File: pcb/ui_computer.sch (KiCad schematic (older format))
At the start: 9 parts

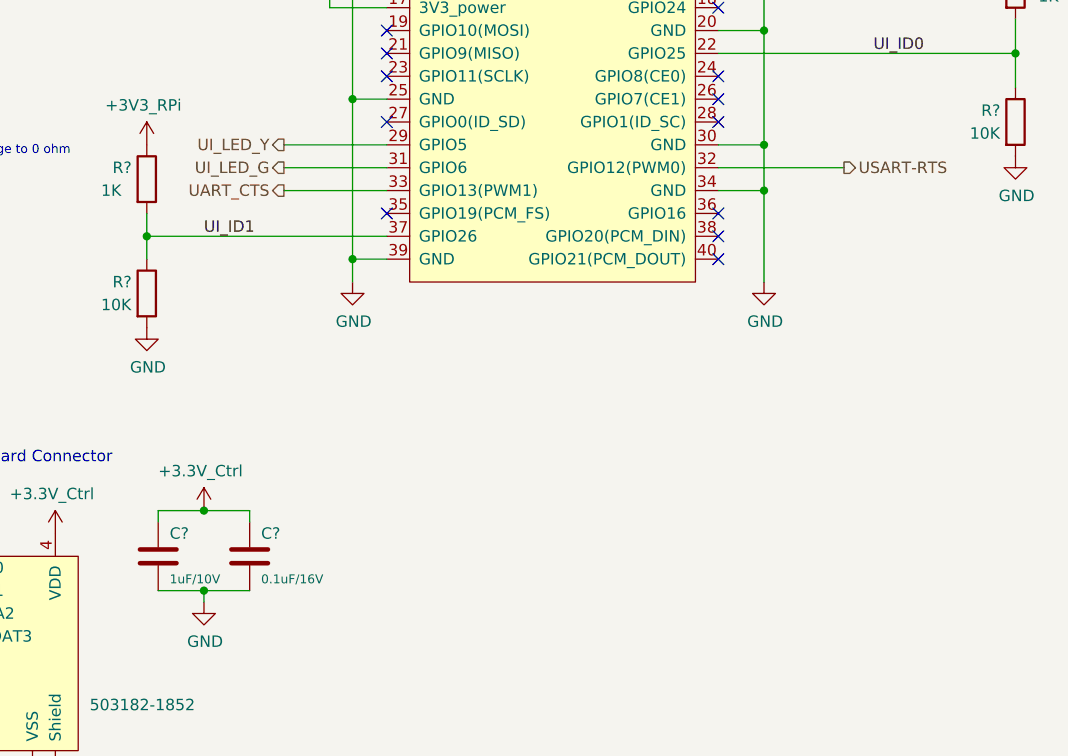
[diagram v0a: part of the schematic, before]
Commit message: change some I/Os
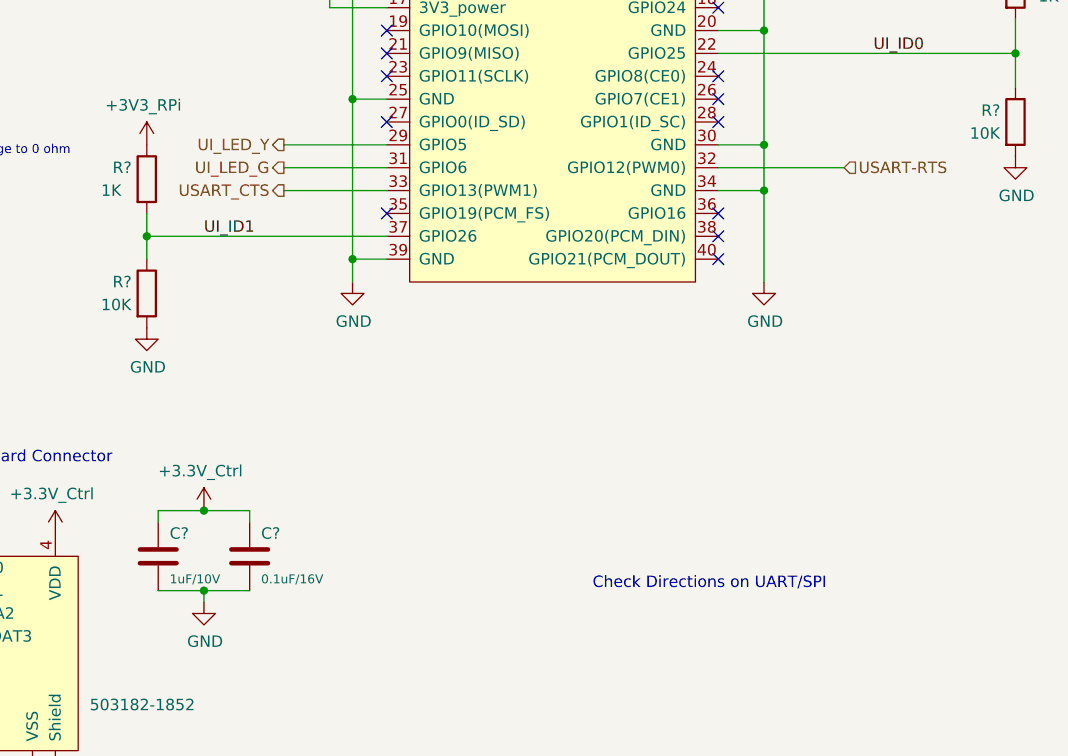
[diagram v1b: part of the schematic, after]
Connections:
- net labels added: USART_CTS
- net labels removed: UART_CTS
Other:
- note added: "Check Directions on UART/SPI"
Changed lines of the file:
@@
 RPI powered by 5V\n
 Text HLabel 4550 3900 0    50   Output ~ 0
-UART_CTS
+USART_CTS
 Wire Wire Line
 	5000 3900 4550 3900
@@
 Wire Wire Line
 	6450 3800 7000 3800
-Text HLabel 7000 3800 2    50   Output ~ 0
+Text HLabel 7000 3800 2    50   Input ~ 0
 USART-RTS
 $Comp
@@
 Text HLabel 2700 6050 0    50   Input ~ 0
 USD-SCLK
+Text Notes 5900 5650 0    50   ~ 0
+Check Directions on UART/SPI
 $EndSCHEMATC

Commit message: started stm
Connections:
- net labels added: +5V_GUI
- net labels removed: +5V_RPi
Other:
- note removed: "RPI has internal I2C pull-ups\n"
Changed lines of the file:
@@
 	1    0    0    -1
 $EndComp
-Text Notes 5200 1950 0    50   ~ 0
-RPI has internal I2C pull-ups\n
 NoConn ~ 5000 2400
 NoConn ~ 5000 2500
@@
 NoConn ~ 5000 3600
 NoConn ~ 5000 4000
-$Comp
-L RespiraWorks:+5V_RPi #PWR?
-U 1 1 5FE675EB
-P 6750 2300
-F 0 "#PWR?" H 6750 2300 50  0001 C CNN
-F 1 "+5V_RPi" H 6735 2473 50  0000 C CNN
-F 2 "" H 6750 2300 50  0001 C CNN
-F 3 "" H 6750 2300 50  0001 C CNN
-	1    6750 2300
-	1    0    0    -1
-$EndComp
 Wire Wire Line
 	6450 2300 6750 2300
@@
 Wire Wire Line
 	6750 2400 6750 2300
-Connection ~ 6750 2300
 Wire Wire Line
 	6650 4300 6650 3900
@@
 Text Notes 5900 5650 0    50   ~ 0
 Check Directions on UART/SPI
+$Comp
+L RespiraWorks:+5V_GUI #PWR?
+U 1 1 5FEBC42B
+P 6750 2300
+F 0 "#PWR?" H 6750 2300 50  0001 C CNN
+F 1 "+5V_GUI" H 6735 2473 50  0000 C CNN
+F 2 "" H 6750 2300 50  0001 C CNN
+F 3 "" H 6750 2300 50  0001 C CNN
+	1    6750 2300
+	1    0    0    -1
+$EndComp
+Connection ~ 6750 2300
 $EndSCHEMATC

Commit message: most up to date
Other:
- note added: "Place USB to UART for FPGA comms"
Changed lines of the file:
@@
 $EndComp
 Connection ~ 6750 2300
+Text Notes 2450 1850 0    50   ~ 0
+Place USB to UART for FPGA comms
 $EndSCHEMATC

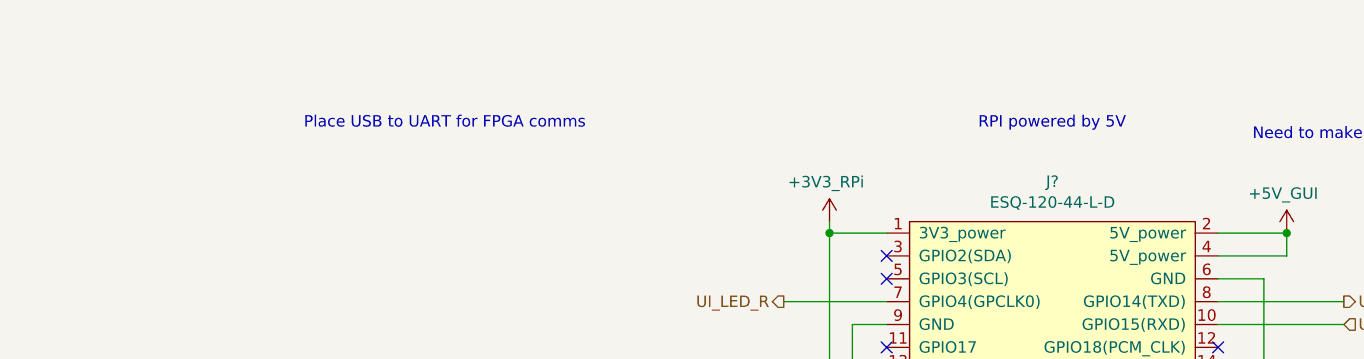
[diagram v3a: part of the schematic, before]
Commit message: updated cycle controller
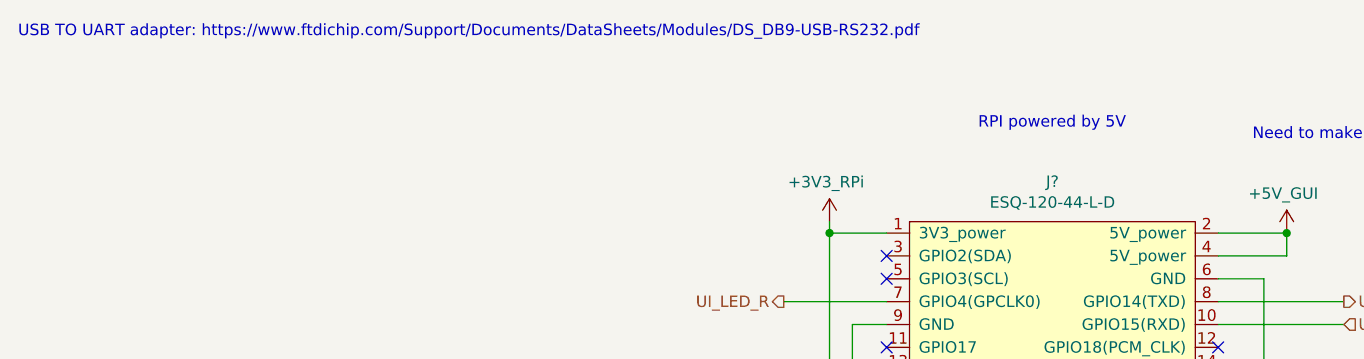
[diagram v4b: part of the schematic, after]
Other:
- note added: "USB TO UART adapter: https://www.ftdichip.com/Support/Documents/DataSheets/Modules/DS_DB9-USB-RS232.pdf"
- note removed: "Place USB to UART for FPGA comms"
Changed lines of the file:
@@
 $Descr A4 11693 8268
 encoding utf-8
-Sheet 14 14
+Sheet 6 28
 Title "UI Computer"
 Date ""
@@
 $EndComp
 Connection ~ 6750 2300
-Text Notes 2450 1850 0    50   ~ 0
-Place USB to UART for FPGA comms
+Text Notes 1200 1450 0    50   ~ 0
+USB TO UART adapter: https://www.ftdichip.com/Support/Documents/DataSheets/Modules/DS_DB9-USB-RS232.pdf
 $EndSCHEMATC

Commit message: some cycle controller updates- more to come shortly
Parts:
- removed C?: 1uF/10V, symbol Device:C
- removed C?: 0.1uF/16V, symbol Device:C
- removed J?: 503182-1852, RespiraWorks:5031821852, symbol RespiraWorks:503182-1852
- removed R?: 10K, RespiraWorks_std:R_0603_1608Metric, symbol Device:R
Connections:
- no-connect marks 21 -> 18
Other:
- note removed: "Check Directions on UART/SPI"
- note removed: "Double Check sw/dt footprint"
- note removed: "MicroSD Card Connector"
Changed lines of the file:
@@
 USART-RTS
-$Comp
-L RespiraWorks:503182-1852 J?
-U 1 1 5FE6F067
-P 3350 5800
-F 0 "J?" H 3150 6150 50  0000 L CNN
-F 1 "503182-1852" H 3700 5450 50  0000 L CNN
-F 2 "RespiraWorks:5031821852" H 4150 5400 50  0001 C CNN
-F 3 "https://www.molex.com/pdm_docs/sd/5031821852_sd.pdf" H 4750 5300 50  0001 C CNN
-	1    3350 5800
-	1    0    0    -1
-$EndComp
-Text Notes 3800 5100 2    50   ~ 0
-MicroSD Card Connector
-$Comp
-L RespiraWorks:+3.3V_Ctrl #PWR?
-U 1 1 5FE6F137
-P 3550 5400
-F 0 "#PWR?" H 3550 5400 50  0001 C CNN
-F 1 "+3.3V_Ctrl" H 3535 5573 50  0000 C CNN
-F 2 "" H 3550 5400 50  0001 C CNN
-F 3 "" H 3550 5400 50  0001 C CNN
-	1    3550 5400
-	1    0    0    -1
-$EndComp
-$Comp
-L Device:C C?
-U 1 1 5FE6F180
-P 4000 5500
-F 0 "C?" H 4050 5600 50  0000 L CNN
-F 1 "1uF/10V" H 4050 5400 39  0000 L CNN
-F 2 "" H 4038 5350 50  0001 C CNN
-F 3 "~" H 4000 5500 50  0001 C CNN
-	1    4000 5500
-	1    0    0    -1
-$EndComp
-$Comp
-L Device:C C?
-U 1 1 5FE6F1C6
-P 4400 5500
-F 0 "C?" H 4450 5600 50  0000 L CNN
-F 1 "0.1uF/16V" H 4450 5400 39  0000 L CNN
-F 2 "" H 4438 5350 50  0001 C CNN
-F 3 "~" H 4400 5500 50  0001 C CNN
-	1    4400 5500
-	1    0    0    -1
-$EndComp
-$Comp
-L RespiraWorks:+3.3V_Ctrl #PWR?
-U 1 1 5FE6F2AB
-P 4200 5300
-F 0 "#PWR?" H 4200 5300 50  0001 C CNN
-F 1 "+3.3V_Ctrl" H 4185 5473 50  0000 C CNN
-F 2 "" H 4200 5300 50  0001 C CNN
-F 3 "" H 4200 5300 50  0001 C CNN
-	1    4200 5300
-	1    0    0    -1
-$EndComp
-Wire Wire Line
-	4000 5350 4000 5300
-Wire Wire Line
-	4000 5300 4200 5300
-Wire Wire Line
-	4200 5300 4400 5300
-Wire Wire Line
-	4400 5300 4400 5350
-Connection ~ 4200 5300
-$Comp
-L power:GND #PWR?
-U 1 1 5FE705DA
-P 4200 5700
-F 0 "#PWR?" H 4200 5450 50  0001 C CNN
-F 1 "GND" H 4205 5527 50  0000 C CNN
-F 2 "" H 4200 5700 50  0001 C CNN
-F 3 "" H 4200 5700 50  0001 C CNN
-	1    4200 5700
-	1    0    0    -1
-$EndComp
-Wire Wire Line
-	4000 5650 4200 5650
-Wire Wire Line
-	4200 5650 4200 5700
-Wire Wire Line
-	4400 5650 4200 5650
-Connection ~ 4200 5650
-$Comp
-L power:GND #PWR?
-U 1 1 5FE71557
-P 3500 6500
-F 0 "#PWR?" H 3500 6250 50  0001 C CNN
-F 1 "GND" H 3505 6327 50  0000 C CNN
-F 2 "" H 3500 6500 50  0001 C CNN
-F 3 "" H 3500 6500 50  0001 C CNN
-	1    3500 6500
-	1    0    0    -1
-$EndComp
-Wire Wire Line
-	3500 6500 3550 6500
-Wire Wire Line
-	3550 6500 3550 6450
-Wire Wire Line
-	3450 6450 3450 6500
-Wire Wire Line
-	3450 6500 3500 6500
-Connection ~ 3500 6500
-Text Notes 2600 5350 2    50   ~ 0
-Double Check sw/dt footprint
-NoConn ~ 2900 5650
-NoConn ~ 2900 5750
-NoConn ~ 2900 6150
-Text Label 2600 6250 2    50   ~ 0
-USD-Detect
-Wire Wire Line
-	1900 6250 2900 6250
-Wire Wire Line
-	1900 6250 1900 6100
-$Comp
-L Device:R R?
-U 1 1 5FE79887
-P 1900 5950
-F 0 "R?" H 1750 6000 50  0000 L CNN
-F 1 "10K" H 1700 5900 50  0000 L CNN
-F 2 "RespiraWorks_std:R_0603_1608Metric" V 1830 5950 50  0001 C CNN
-F 3 "~" H 1900 5950 50  0001 C CNN
-	1    1900 5950
-	1    0    0    -1
-$EndComp
-$Comp
-L RespiraWorks:+3.3V_Ctrl #PWR?
-U 1 1 5FE798FA
-P 1900 5800
-F 0 "#PWR?" H 1900 5800 50  0001 C CNN
-F 1 "+3.3V_Ctrl" H 1885 5973 50  0000 C CNN
-F 2 "" H 1900 5800 50  0001 C CNN
-F 3 "" H 1900 5800 50  0001 C CNN
-	1    1900 5800
-	1    0    0    -1
-$EndComp
-Wire Wire Line
-	2900 6050 2700 6050
-Wire Wire Line
-	2900 5950 2700 5950
-Wire Wire Line
-	2900 5850 2700 5850
-Wire Wire Line
-	2900 5550 2700 5550
-Text HLabel 2700 5550 0    50   Output ~ 0
-USD-MISO
-Text HLabel 2700 5850 0    50   Input ~ 0
-USD-CS
-Text HLabel 2700 5950 0    50   Input ~ 0
-USD-MOSI
-Text HLabel 2700 6050 0    50   Input ~ 0
-USD-SCLK
-Text Notes 5900 5650 0    50   ~ 0
-Check Directions on UART/SPI
 $Comp
 L RespiraWorks:+5V_GUI #PWR?

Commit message: ui computer
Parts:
- R? (x2): DNP (none) -> DNP
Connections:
- net USART-RX: now also J?.10 (GPIO15(RXD)); no longer J?.8 (GPIO14(TXD))
- net USART-TX: now also J?.8 (GPIO14(TXD)); no longer J?.10 (GPIO15(RXD))
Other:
- note removed: "Added small R value/ strong pull-up. Can always change to 0 ohm\n"
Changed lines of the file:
@@
 	1    0    0    -1
 $EndComp
-Text Notes 1850 3750 0    39   ~ 0
-Added small R value/ strong pull-up. Can always change to 0 ohm\n
 $Comp
 L RespiraWorks:+3V3_RPi #PWR?
@@
 F 2 "RespiraWorks_std:R_0603_1608Metric" V 3880 3850 50  0001 C CNN
 F 3 "~" H 3950 3850 50  0001 C CNN
+F 4 "DNP" H 3700 3850 50  0000 C CNN "DNP"
 	1    3950 3850
 	1    0    0    -1
@@
 	6450 2600 7000 2600
 Text HLabel 7000 2600 2    50   Output ~ 0
-USART-RX
+USART-TX
 Wire Wire Line
 	6450 2700 7000 2700
 Text HLabel 7000 2700 2    50   Input ~ 0
-USART-TX
+USART-RX
 NoConn ~ 6450 2800
 NoConn ~ 6450 3000
@@
 F 2 "RespiraWorks_std:R_0603_1608Metric" V 7680 3000 50  0001 C CNN
 F 3 "~" H 7750 3000 50  0001 C CNN
+F 4 "DNP" H 7600 3000 50  0000 C CNN "DNP"
 	1    7750 3000
 	1    0    0    -1

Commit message: modified cycle controller and slightly ui
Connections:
- net USART-RTS renamed USART-CTS
- net USART_CTS renamed USART_RTS
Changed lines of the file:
@@
 RPI powered by 5V\n
 Text HLabel 4550 3900 0    50   Output ~ 0
-USART_CTS
+USART_RTS
 Wire Wire Line
 	5000 3900 4550 3900
@@
 	6450 3800 7000 3800
 Text HLabel 7000 3800 2    50   Input ~ 0
-USART-RTS
+USART-CTS
 $Comp
 L RespiraWorks:+5V_GUI #PWR?
